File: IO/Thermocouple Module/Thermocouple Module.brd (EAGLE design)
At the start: 25.4 x 25.4 mm, 3 parts

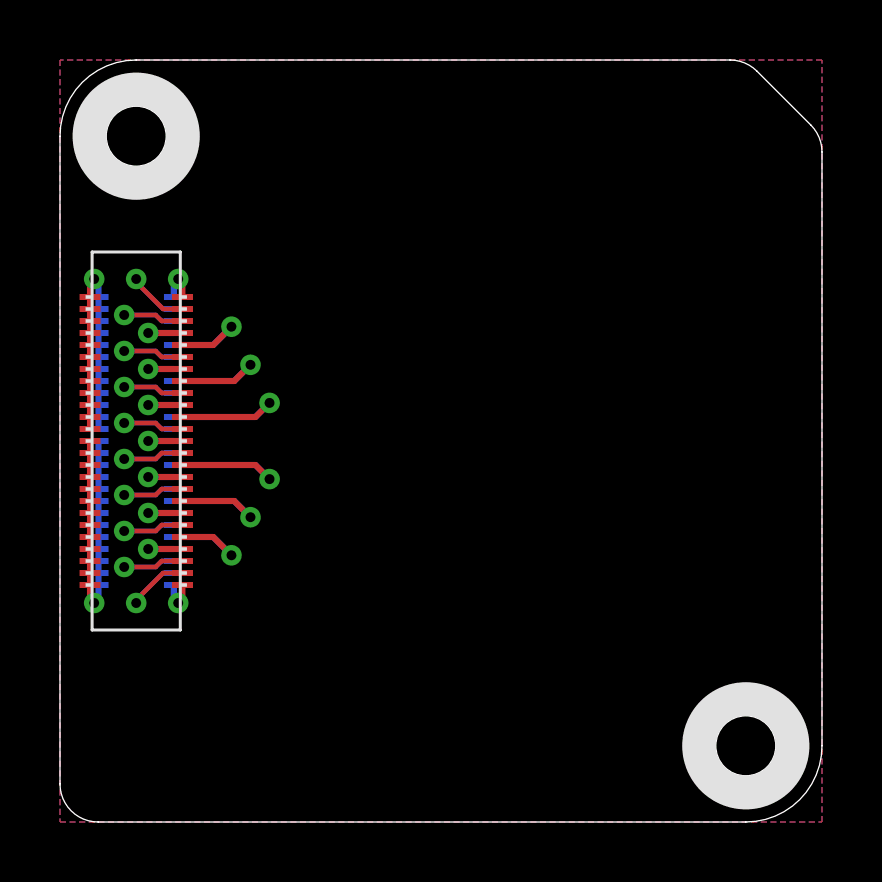
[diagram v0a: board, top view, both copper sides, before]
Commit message: Completed Thermocouple Module
Signed-off-by: Cruz Monrreal II <Cruz.Monrreal@gmail.com>
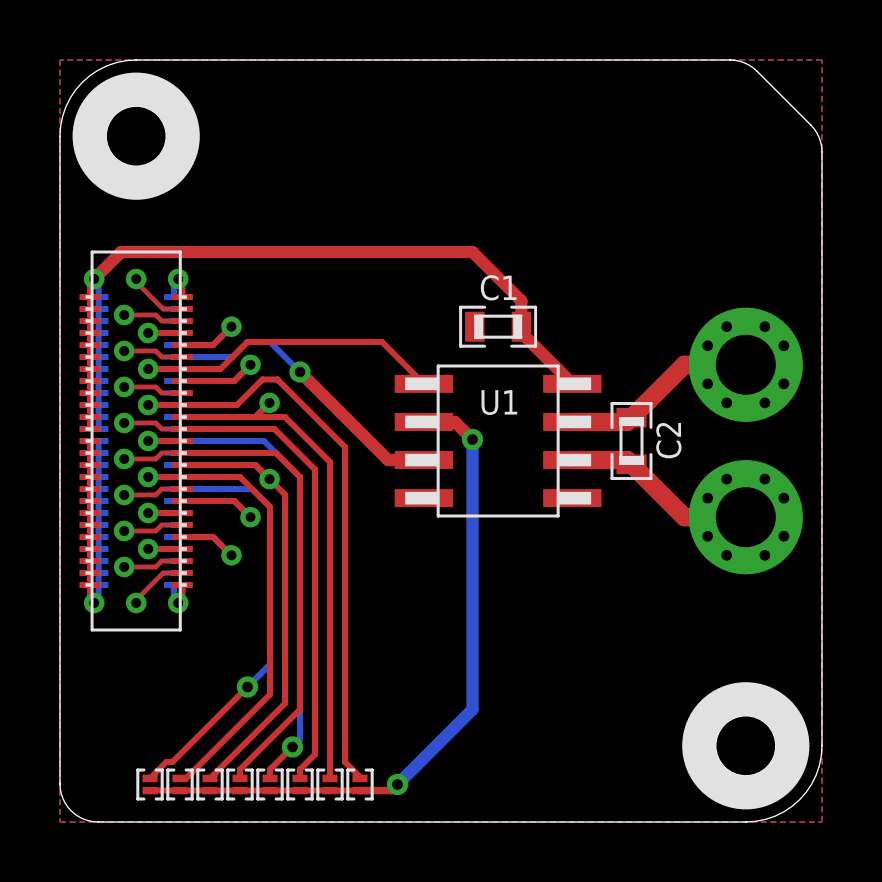
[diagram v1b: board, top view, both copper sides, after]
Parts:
- added C1: .1uF, .standardparts:0603
- added C2: .01uF, .standardparts:0603
- added J1, J2, J3, J4, J5, J6, J7, J8: (no value), .solderjumper:2.SML
- added U1: MAX31855, maxim:SO08
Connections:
- removed net N$6: U$2.MISO, U$2.MISO@1, U$2.MISO@VIA
- removed net N$7: U$2.SCLK, U$2.SCLK@1, U$2.SCLK@VIA
- new net !CS: J1.2, J2.2, J3.2, J4.2, J5.2, J6.2, J7.2, J8.2, U1.6
- new net MISO: U$2.MISO, U$2.MISO@1, U$2.MISO@VIA, U1.7
- new net SCLK: U$2.SCLK, U$2.SCLK@1, U$2.SCLK@VIA, U1.5
- new net T+: C2.1, U1.3
- new net T-: C2.2, U1.2
- net 3.3V: now also C1.1, U1.4
- net GND: now also C1.2, U1.1
- net N$1: now also J1.1, U$2.01, U$2.01@1, U$2.01@VIA; no longer U$2.04, U$2.04@1, U$2.04@VIA
- net N$10: now also J3.1, U$2.03, U$2.03@1, U$2.03@VIA; no longer U$2.01, U$2.01@1, U$2.01@VIA
- net N$11: now also J4.1, U$2.04, U$2.04@1, U$2.04@VIA; no longer U$2.02, U$2.02@1, U$2.02@VIA
- net N$14: now also J5.1
- net N$15: now also J6.1
- net N$16: now also J7.1
- net N$17: now also J8.1
- net N$5: now also J2.1, U$2.02, U$2.02@1, U$2.02@VIA; no longer U$2.03, U$2.03@1, U$2.03@VIA
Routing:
- net !CS: track 0.00 -> 22.7 mm, vias 0 -> 2
- net 3.3V: track 0.00 -> 18.8 mm
- net N$1: track 0.00 -> 18.0 mm
- net N$10: track 0.00 -> 15.5 mm
- net N$11: track 0.00 -> 15.2 mm, vias 0 -> 1
- net N$14: track 0.00 -> 15.1 mm
- net N$17: track 0.00 -> 14.3 mm, vias 0 -> 1
- net N$16: track 0.00 -> 13.7 mm
- net N$5: track 0.00 -> 13.7 mm
- net N$15: track 0.00 -> 11.2 mm
- net MISO: track 0.00 -> 10.2 mm, vias 0 -> 1
- net SCLK: track 0.00 -> 9.00 mm
- net T-: track 0.00 -> 6.57 mm, vias 0 -> 9
- net T+: track 0.00 -> 6.57 mm, vias 0 -> 9
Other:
- board text added: "01"
- board text added: "02"
- board text added: "03"
- board text added: "04"
- board text added: "05"
- board text added: "06"
- board text added: "07"
- board text added: "08"
- board text added: "CS"
